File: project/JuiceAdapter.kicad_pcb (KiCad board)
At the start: 2 copper layers, 24 x 10 mm, 6 parts, among them J1 Conn_01x04_Pin, J2 Conn_01x04_Pin, Q1 MMDT5401

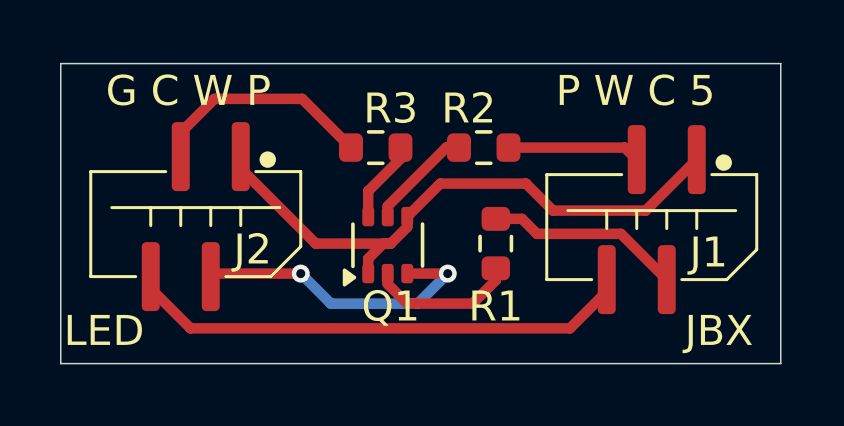
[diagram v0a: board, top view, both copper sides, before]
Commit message: Adjusted traces for single-sided board
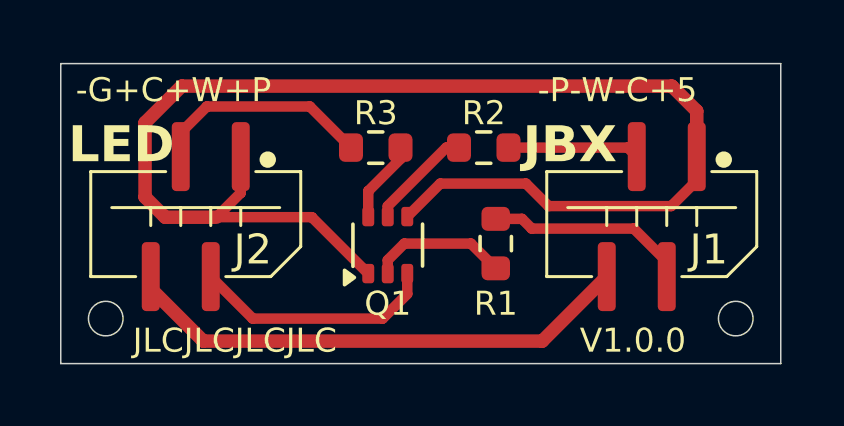
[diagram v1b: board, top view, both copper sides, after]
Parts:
- moved J1 0.10 mm to (137.2, 99.6)
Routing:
- net Net-(J1-Pin_1): track 20.2 -> 45.7 mm
- net Net-(J2-Pin_2): track 10.1 -> 8.29 mm, vias 2 -> 0
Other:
- outline, holes or cut-outs redrawn
- board text added: "-G+C+W+P"
- board text added: "-P-W-C+5"
- board text added: "JLCJLCJLCJLC"
- board text added: "V1.0.0"
- board text removed: "G C W P"
- board text removed: "P W C 5"
